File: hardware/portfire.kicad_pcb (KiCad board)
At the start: 2 copper layers, 100 x 100 mm, 200 parts, among them IC101 STM32F407VGT6TR, IC102 TPS62152, IC103 25AA02E48, IC104 ADP3335, IC105 SNx5176B, IC201 MAX5969x, IC202 KSZ8081RNA, IC203 MAX17503, IC301 TPS92512, J201 RJ45, J202 AUX POWER, P101 SWD_TC, P102 AUX_BUS_RX, P103 AUX_BUS_RX, P301 1, P302 2, P303 3, P304 4, P305 5, P306 6, P307 7, P308 8, P309 9, P310 10, P311 11, P312 12, P313 13, P314 14, P315 15, P316 16, P317 17, P318 18, P319 19, P320 20, P321 21, P322 22, P323 23, P324 24, P325 25, P326 26, P327 27, P328 28, P329 29, P330 30, Q301 NTR4501NT1G, Q302 NTR4501NT1G, Q303 NTR4501NT1G, Q304 NTR4501NT1G, Q305 NTR4501NT1G, Q306 NTR4501NT1G, Q307 NTR4501NT1G, Q308 NTR4501NT1G, Q309 NTR4501NT1G, Q310 NTR4501NT1G, Q311 NTR4501NT1G, Q312 NTR4501NT1G, Q313 NTR4501NT1G, Q314 NTR4501NT1G, Q315 NTR4501NT1G, Q316 NTR4501NT1G, Q317 NTR4501NT1G, Q318 NTR4501NT1G, Q319 NTR4501NT1G, Q320 NTR4501NT1G, Q321 NTR4501NT1G, Q322 NTR4501NT1G, Q323 NTR4501NT1G, Q324 NTR4501NT1G, Q325 NTR4501NT1G, Q326 NTR4501NT1G, Q327 NTR4501NT1G, Q328 NTR4501NT1G, Q329 NTR4501NT1G, Q330 NTR4501NT1G, T201 749010012A, X101 PART, X102 PART, X103 PART, X104 PART, Y101 26M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

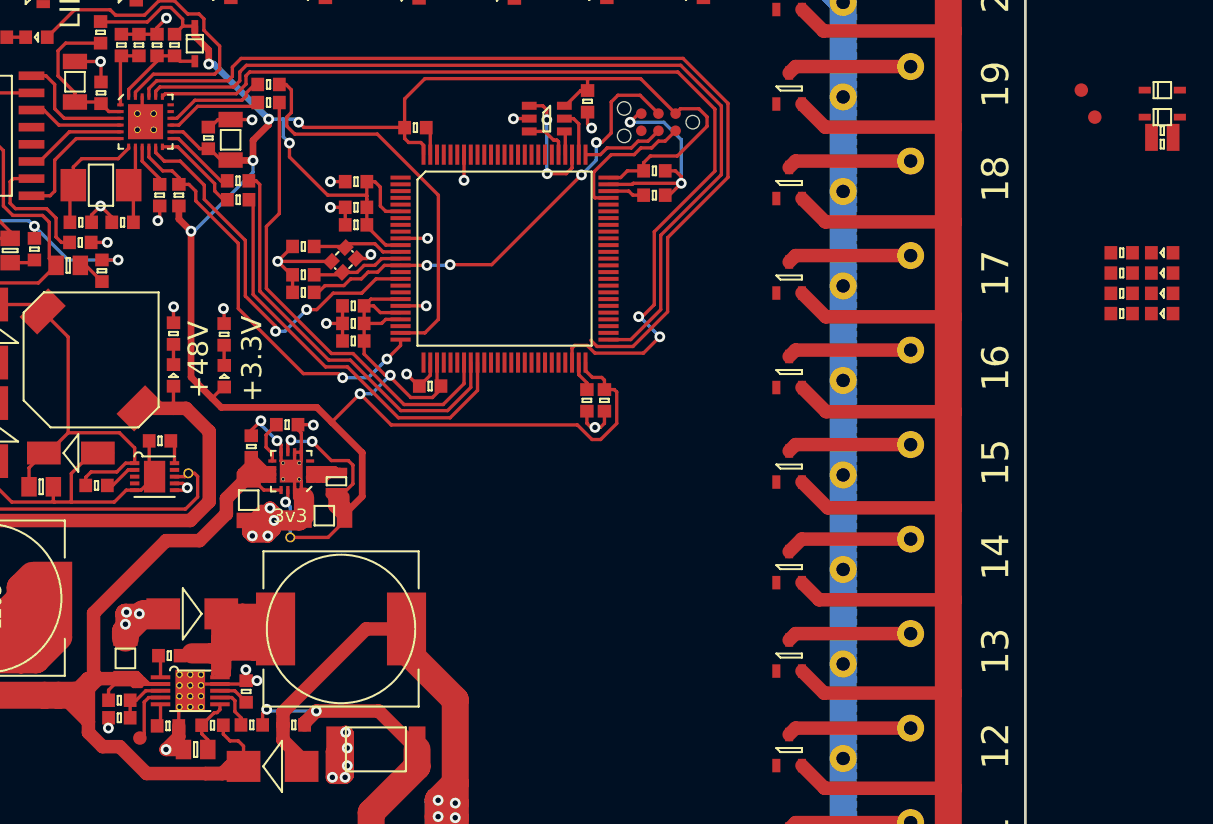
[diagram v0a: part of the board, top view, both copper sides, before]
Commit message: Routed cont, arm, LEDs
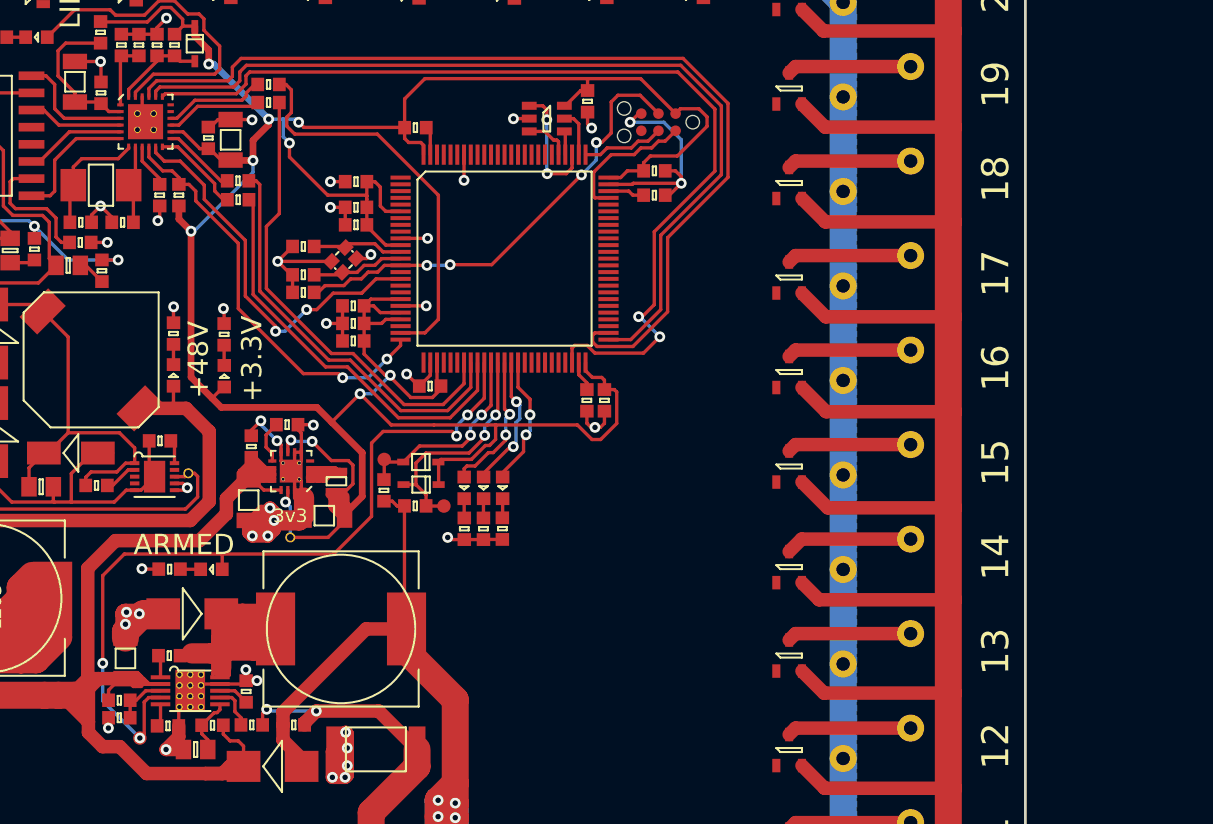
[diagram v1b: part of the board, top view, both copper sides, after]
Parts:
- moved R107 73.4 mm to (79.3, 104.8), turned to 180 degrees
- moved D107 73.3 mm to (82.4, 104.8)
- moved R306 63.1 mm to (95.1, 98.9), turned to 270 degrees
- moved D301 62.2 mm to (97.9, 98.5), turned to 180 degrees
- moved R304 61.9 mm to (97.5, 100.1)
- moved D302 60.6 mm to (97.9, 96.8), turned to 180 degrees
- moved TP303 58.4 mm to (95.2, 96.6), turned to 180 degrees
- moved TP301 56.4 mm to (99.6, 100.1), turned to 180 degrees
- moved D108 54.1 mm to (101.1, 98.7), turned to 90 degrees
- moved D109 53.2 mm to (102.5, 98.7), turned to 90 degrees
- moved R108 52.2 mm to (101.1, 101.8), turned to 270 degrees
- moved R109 51.5 mm to (102.5, 101.8), turned to 270 degrees
- moved D106 50.5 mm to (103.9, 98.7), turned to 90 degrees
- moved R106 48.6 mm to (103.9, 101.8), turned to 270 degrees
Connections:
- D106 pad 2: (no net) -> /TRAFFIC
- D107 pad 2: (no net) -> /ARM
- D108 pad 2: (no net) -> /STATUS
- D109 pad 2: (no net) -> /ERROR
- D301 pad 2: /firing/CONT_EN -> /CONT_EN
- D302 pad 2: /firing/CONT -> /CONT
- IC101 pad 35: (no net) -> /ARM
- IC101 pad 36: (no net) -> /CONT
- IC101 pad 37: (no net) -> /CONT_EN
- IC101 pad 38: (no net) -> /STATUS
- IC101 pad 39: (no net) -> /ERROR
- IC101 pad 40: (no net) -> /TRAFFIC
- IC301 pad 4: /firing/ARM -> /ARM
- R304 pad 2: /firing/CONT_EN -> /CONT_EN
- R306 pad 1: /firing/CONT -> /CONT
- TP301 pad 1: /firing/CONT_EN -> /CONT_EN
- TP302 pad 1: /firing/ARM -> /ARM
- TP303 pad 1: /firing/CONT -> /CONT
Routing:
- net /ARM: track 0.00 -> 59.0 mm, vias 0 -> 4
- net /CONT_EN: track 0.00 -> 17.6 mm, vias 0 -> 2
- net /CONT: track 0.00 -> 14.9 mm, vias 0 -> 2
- net /firing/BUS: track 269.7 -> 280.6 mm
- net /STATUS: track 0.00 -> 10.6 mm, vias 0 -> 2
- net /ERROR: track 0.00 -> 9.99 mm, vias 0 -> 2
- net /TRAFFIC: track 0.00 -> 9.69 mm, vias 0 -> 2
- net 3v3: track 224.6 -> 232.3 mm
- net GND: track 208.2 -> 213.6 mm, vias 59 -> 61
- net /firing/ARM: track 4.14 -> 0.00 mm
- net +6V: track 146.0 -> 148.3 mm
- net /RMII_TXD1: track 70.4 -> 72.0 mm
- net Net-(D107-Pad1): track 0.00 -> 1.50 mm
- net Net-(D109-Pad1): track 0.00 -> 1.43 mm
- net Net-(D108-Pad1): track 0.00 -> 1.43 mm
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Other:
- board text added: "ARMED"

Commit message: Routed firing channels
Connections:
- IC101 pad 26: (no net) -> /AUX_BUS_RX
- IC101 pad 41: (no net) -> /CH7
- IC101 pad 42: (no net) -> /CH6
- IC101 pad 43: (no net) -> /CH5
- IC101 pad 44: (no net) -> /CH4
- IC101 pad 45: (no net) -> /CH3
- IC101 pad 46: (no net) -> /CH2
- IC101 pad 47: (no net) -> /CH1
- IC101 pad 53: (no net) -> /CH8
- IC101 pad 54: (no net) -> /CH9
- IC101 pad 55: (no net) -> /CH10
- IC101 pad 56: (no net) -> /CH11
- IC101 pad 58: (no net) -> /CH12
- IC101 pad 59: (no net) -> /CH13
- IC101 pad 60: (no net) -> /CH14
- IC101 pad 61: (no net) -> /CH15
- IC101 pad 63: (no net) -> /CH16
- IC101 pad 64: (no net) -> /CH17
- IC101 pad 65: (no net) -> /CH18
- IC101 pad 67: (no net) -> /CH19
- IC101 pad 68: (no net) -> /CH20
- IC101 pad 69: (no net) -> /CH21
- IC101 pad 89: (no net) -> /CH22
- IC101 pad 90: (no net) -> /CH23
- IC101 pad 91: (no net) -> /CH24
- IC101 pad 92: (no net) -> /CH25
- IC101 pad 93: (no net) -> /CH26
- IC101 pad 95: (no net) -> /CH30
- IC101 pad 96: (no net) -> /CH29
- IC101 pad 97: (no net) -> /CH28
- IC101 pad 98: (no net) -> /CH27
- IC105 pad 1: (no net) -> /AUX_BUS_RX
- Q301 pad 1: (no net) -> /CH1
- Q302 pad 1: (no net) -> /CH2
- Q303 pad 1: (no net) -> /CH3
- Q304 pad 1: (no net) -> /CH4
- Q305 pad 1: (no net) -> /CH5
- Q306 pad 1: (no net) -> /CH6
- Q307 pad 1: (no net) -> /CH7
- Q308 pad 1: (no net) -> /CH8
- Q309 pad 1: (no net) -> /CH9
- Q310 pad 1: (no net) -> /CH10
- Q311 pad 1: (no net) -> /CH11
- Q312 pad 1: (no net) -> /CH12
- Q313 pad 1: (no net) -> /CH13
- Q314 pad 1: (no net) -> /CH14
- Q315 pad 1: (no net) -> /CH15
- Q316 pad 1: (no net) -> /CH16
- Q317 pad 1: (no net) -> /CH17
- Q318 pad 1: (no net) -> /CH18
- Q319 pad 1: (no net) -> /CH19
- Q320 pad 1: (no net) -> /CH20
- Q321 pad 1: (no net) -> /CH21
- Q322 pad 1: (no net) -> /CH22
- Q323 pad 1: (no net) -> /CH23
- Q324 pad 1: (no net) -> /CH24
- Q325 pad 1: (no net) -> /CH25
- Q326 pad 1: (no net) -> /CH26
- Q327 pad 1: (no net) -> /CH27
- Q328 pad 1: (no net) -> /CH28
- Q329 pad 1: (no net) -> /CH29
- Q330 pad 1: (no net) -> /CH30
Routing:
- net /AUX_BUS_RX: track 0.00 -> 110.9 mm, vias 0 -> 4
- net /CH1: track 0.00 -> 92.2 mm, vias 0 -> 2
- net /CH2: track 0.00 -> 83.2 mm, vias 0 -> 2
- net /CH3: track 0.00 -> 75.4 mm, vias 0 -> 2
- net /CH4: track 0.00 -> 67.0 mm, vias 0 -> 2
- net /CH30: track 0.00 -> 62.9 mm, vias 0 -> 2
- net /CH5: track 0.00 -> 58.6 mm, vias 0 -> 2
- net /CH29: track 0.00 -> 54.4 mm, vias 0 -> 2
- net /CH11: track 0.00 -> 52.3 mm, vias 0 -> 2
- net /CH6: track 0.00 -> 50.3 mm, vias 0 -> 2
- net /CH8: track 0.00 -> 47.6 mm, vias 0 -> 2
- net /CH10: track 0.00 -> 47.6 mm, vias 0 -> 2
- net /CH28: track 0.00 -> 46.4 mm, vias 0 -> 2
- net /CH12: track 0.00 -> 44.3 mm, vias 0 -> 2
- net /CH9: track 0.00 -> 43.7 mm, vias 0 -> 2
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
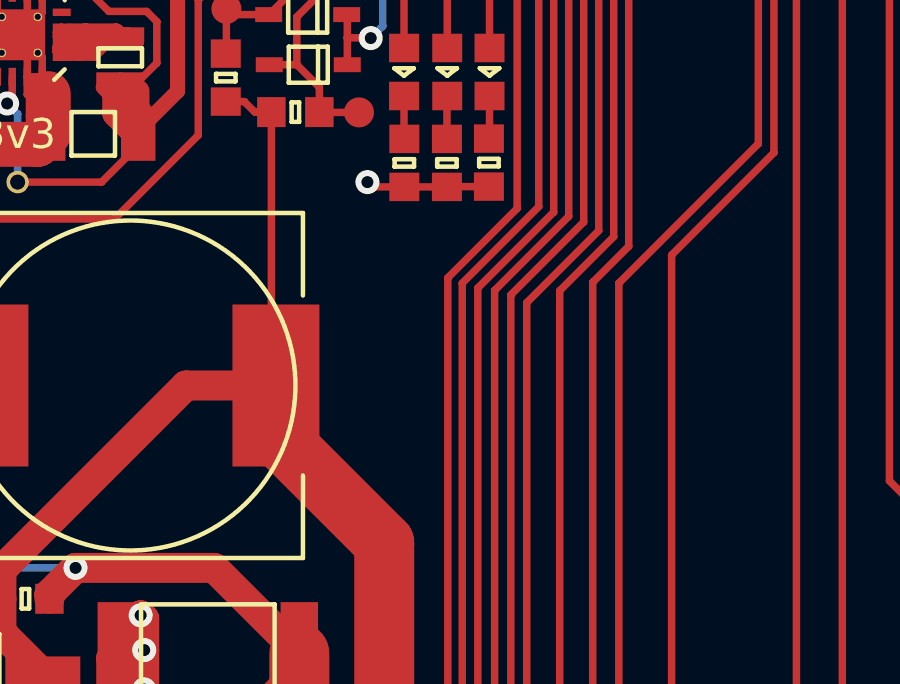
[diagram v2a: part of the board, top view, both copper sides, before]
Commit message: LED labels
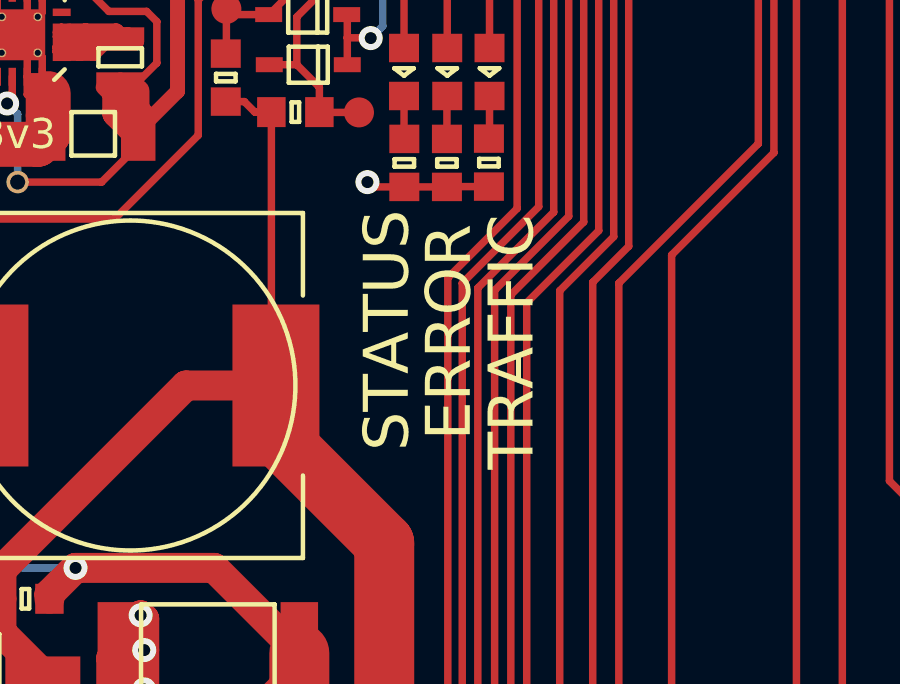
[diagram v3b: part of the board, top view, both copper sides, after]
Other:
- board text added: "ERROR"
- board text added: "STATUS"
- board text added: "TRAFFIC"
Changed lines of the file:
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@@
     (area 42.559999 43.549999 142.760001 143.750001)
     (thickness 1.6)
-    (drawings 15)
+    (drawings 18)
     (tracks 2071)
     (zones 0)
@@
     )
   )
+  (gr_text TRAFFIC (at 104.68 107.73 90) (layer F.SilkS)
+    (effects (font (size 1.5 1.5) (thickness 0.3)))
+  )
+  (gr_text ERROR (at 102.59 107.4 90) (layer F.SilkS)
+    (effects (font (size 1.5 1.5) (thickness 0.3)))
+  )
+  (gr_text STATUS (at 100.52 107.34 90) (layer F.SilkS)
+    (effects (font (size 1.5 1.5) (thickness 0.3)))
+  )
   (gr_text ARMED (at 80.34 102.94) (layer F.SilkS)

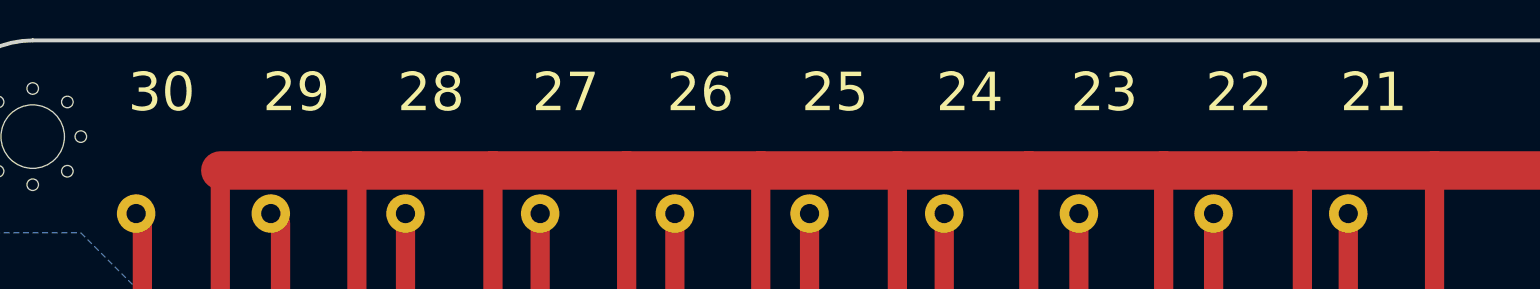
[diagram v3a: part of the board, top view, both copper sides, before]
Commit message: Rotate silk labels on CH21-30
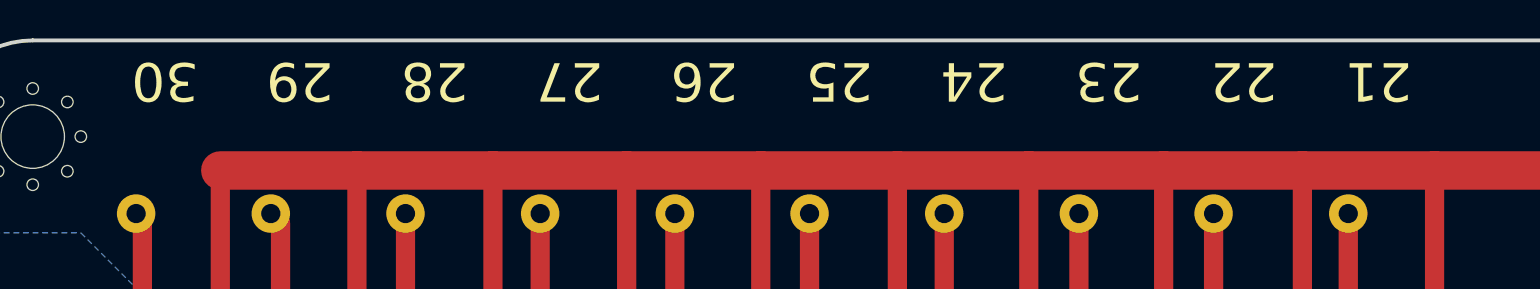
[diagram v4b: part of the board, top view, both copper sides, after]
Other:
- board text added: "21"
- board text added: "22"
- board text added: "23"
- board text added: "24"
- board text added: "25"
- board text added: "26"
- board text added: "27"
- board text added: "28"
- board text added: "29"
- board text added: "30"
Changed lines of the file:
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@@
     (area 42.559999 43.549999 142.760001 143.750001)
     (thickness 1.6)
-    (drawings 18)
+    (drawings 28)
     (tracks 2071)
     (zones 0)
@@
     (pad_to_mask_clearance 0)
     (aux_axis_origin 0 0)
-    (visible_elements FFFCFF7F)
+    (visible_elements FFFEFF7F)
     (pcbplotparams
       (layerselection 0x00030_80000001)
@@
       (effects (font (size 1 1) (thickness 0.15)))
     )
-    (fp_text value 21 (at -0.2 8.8 180) (layer F.SilkS)
+    (fp_text value 21 (at -0.2 8.8 180) (layer F.SilkS) hide
       (effects (font (size 2 2) (thickness 0.3)))
     )
@@
       (effects (font (size 1 1) (thickness 0.15)))
     )
-    (fp_text value 22 (at -0.2 8.8 180) (layer F.SilkS)
+    (fp_text value 22 (at -0.2 8.8 180) (layer F.SilkS) hide
       (effects (font (size 2 2) (thickness 0.3)))
     )
@@
       (effects (font (size 1 1) (thickness 0.15)))
     )
-    (fp_text value 23 (at -0.2 8.8 180) (layer F.SilkS)
+    (fp_text value 23 (at -0.2 8.8 180) (layer F.SilkS) hide
       (effects (font (size 2 2) (thickness 0.3)))
     )
@@
       (effects (font (size 1 1) (thickness 0.15)))
     )
-    (fp_text value 24 (at -0.2 8.8 180) (layer F.SilkS)
+    (fp_text value 24 (at -0.2 8.8 180) (layer F.SilkS) hide
       (effects (font (size 2 2) (thickness 0.3)))
     )
@@
       (effects (font (size 1 1) (thickness 0.15)))
     )
-    (fp_text value 25 (at -0.2 8.8 180) (layer F.SilkS)
+    (fp_text value 25 (at -0.2 8.8 180) (layer F.SilkS) hide
       (effects (font (size 2 2) (thickness 0.3)))
     )
@@
       (effects (font (size 1 1) (thickness 0.15)))
     )
-    (fp_text value 26 (at -0.2 8.8 180) (layer F.SilkS)
+    (fp_text value 26 (at -0.2 8.8 180) (layer F.SilkS) hide
       (effects (font (size 2 2) (thickness 0.3)))
     )
@@
       (effects (font (size 1 1) (thickness 0.15)))
     )
-    (fp_text value 27 (at -0.2 8.8 180) (layer F.SilkS)
+    (fp_text value 27 (at -0.2 8.8 180) (layer F.SilkS) hide
       (effects (font (size 2 2) (thickness 0.3)))
     )
@@
       (effects (font (size 1 1) (thickness 0.15)))
     )
-    (fp_text value 28 (at -0.2 8.8 180) (layer F.SilkS)
+    (fp_text value 28 (at -0.2 8.8 180) (layer F.SilkS) hide
       (effects (font (size 2 2) (thickness 0.3)))
     )
@@
       (effects (font (size 1 1) (thickness 0.15)))
     )
-    (fp_text value 29 (at -0.2 8.8 180) (layer F.SilkS)
+    (fp_text value 29 (at -0.2 8.8 180) (layer F.SilkS) hide
       (effects (font (size 2 2) (thickness 0.3)))
     )
@@
       (effects (font (size 1 1) (thickness 0.15)))
     )
-    (fp_text value 30 (at -0.2 8.8 180) (layer F.SilkS)
+    (fp_text value 30 (at -0.2 8.8 180) (layer F.SilkS) hide
       (effects (font (size 2 2) (thickness 0.3)))
     )
@@
       (net 86 "Net-(P330-Pad2)"))
     (model PTSA0,52-2,5-z.wrl
-      (at (xyz -0.7539370078740157 -0.3622047244094488 -0.7125984251968505))
+      (at (xyz -0.753937 -0.362205 -0.712598))
       (scale (xyz 0.3937 0.3937 0.3937))
       (rotate (xyz -90 0 -90))
@@
     )
   )
+  (gr_text 22 (at 110.593328 45.76 180) (layer F.SilkS)
+    (effects (font (size 2 2) (thickness 0.3)))
+  )
+  (gr_text 24 (at 96.579996 45.76 180) (layer F.SilkS)
+    (effects (font (size 2 2) (thickness 0.3)))
+  )
+  (gr_text 26 (at 82.566664 45.76 180) (layer F.SilkS)
+    (effects (font (size 2 2) (thickness 0.3)))
+  )
+  (gr_text 21 (at 117.599994 45.76 180) (layer F.SilkS)
+    (effects (font (size 2 2) (thickness 0.3)))
+  )
+  (gr_text 23 (at 103.586662 45.76 180) (layer F.SilkS)
+    (effects (font (size 2 2) (thickness 0.3)))
+  )
+  (gr_text 25 (at 89.57333 45.76 180) (layer F.SilkS)
+    (effects (font (size 2 2) (thickness 0.3)))
+  )
+  (gr_text 27 (at 75.559998 45.76 180) (layer F.SilkS)
+    (effects (font (size 2 2) (thickness 0.3)))
+  )
+  (gr_text 28 (at 68.553332 45.76 180) (layer F.SilkS)
+    (effects (font (size 2 2) (thickness 0.3)))
+  )
+  (gr_text 29 (at 61.546666 45.76 180) (layer F.SilkS)
+    (effects (font (size 2 2) (thickness 0.3)))
+  )
+  (gr_text 30 (at 54.54 45.76 180) (layer F.SilkS)
+    (effects (font (size 2 2) (thickness 0.3)))
+  )
   (gr_text TRAFFIC (at 104.68 107.73 90) (layer F.SilkS)
